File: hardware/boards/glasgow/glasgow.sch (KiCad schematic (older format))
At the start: 89 parts, among them J1 USB_B_Micro, U1 CY7C68013A-56LTX, U15 TPD3S014, U2 CAT24M01W, U3 CAT24C256W, U30 ICE40HX8K-BG121, U34 ATECC508A, U7 LM3880MF-1AF, U8 MIC5355-S4YMME, Y1 24M

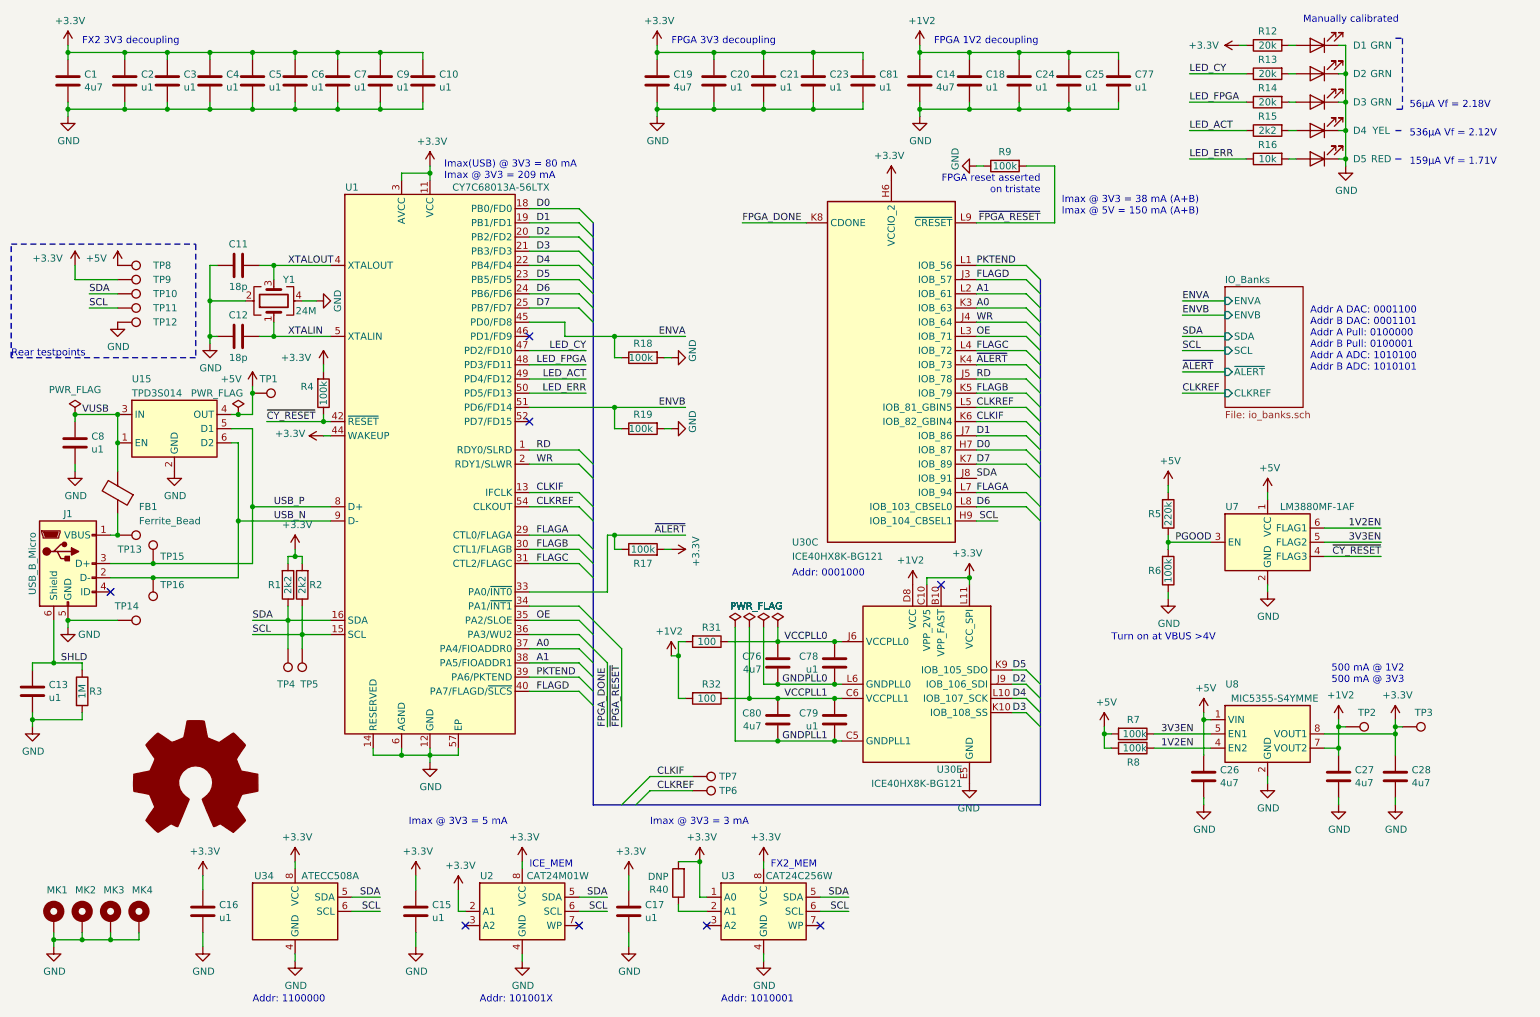
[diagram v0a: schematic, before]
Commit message: revC: add a few detailed explanations on schematic.
Also, where applicable, move text to match moved symbols, and remove
clearly outdated text.
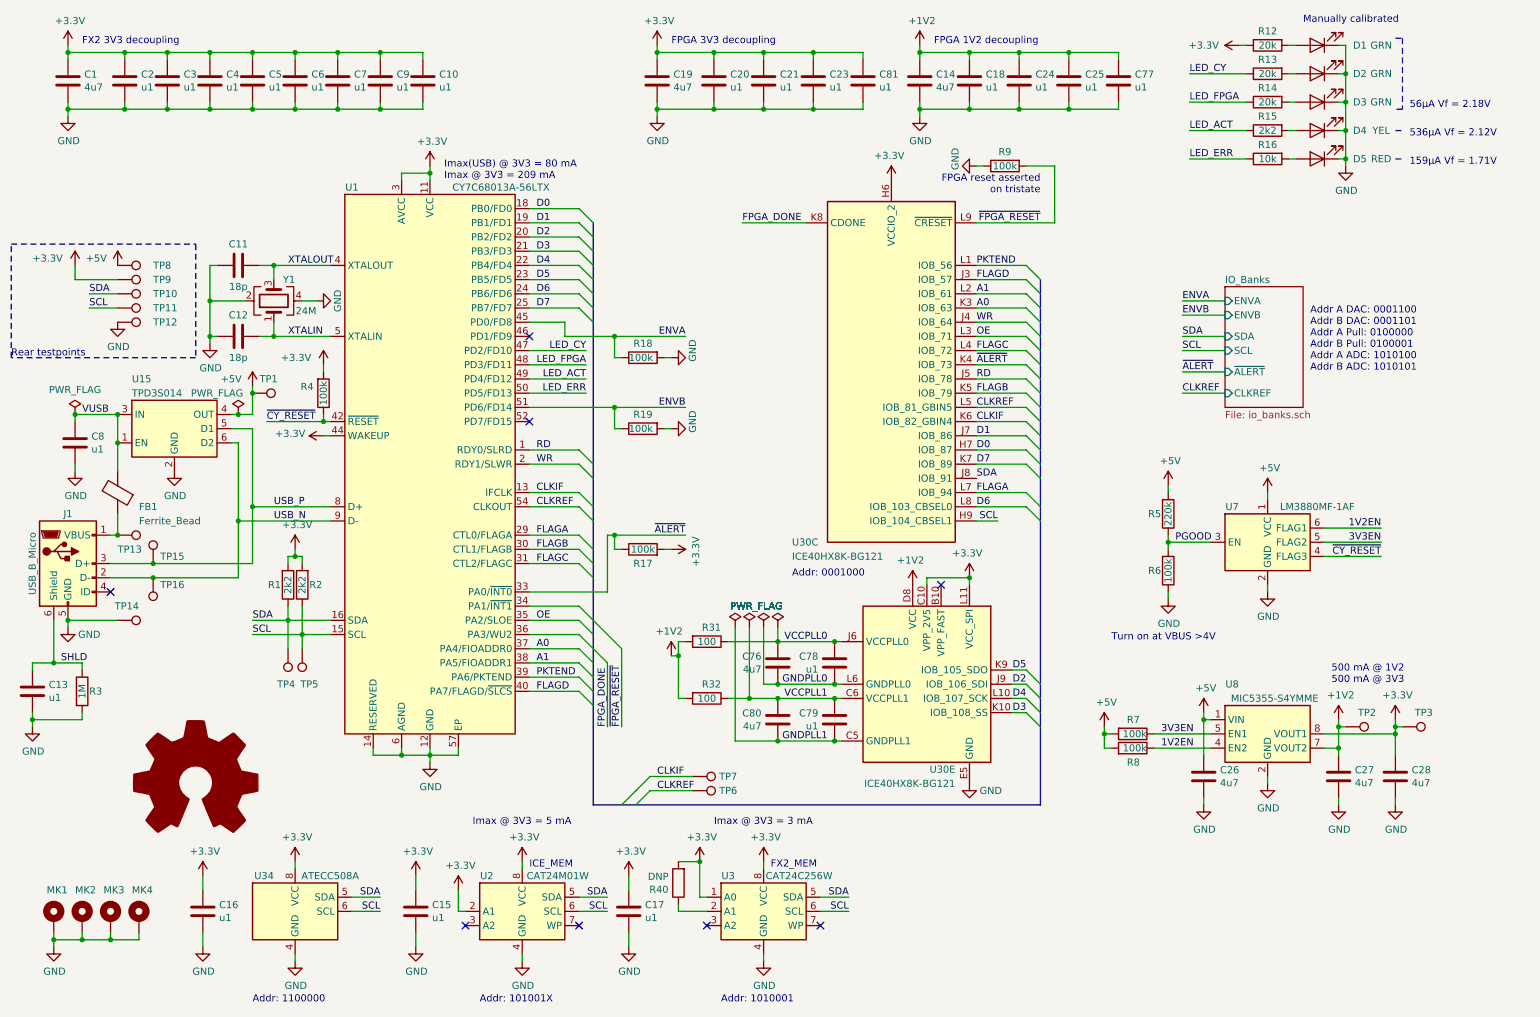
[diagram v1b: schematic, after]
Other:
- note removed: "Imax @ 3V3 = 38 mA (A+B)\nImax @ 5V = 150 mA (A+B)"
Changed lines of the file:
@@
 EESchema Schematic File Version 4
 LIBS:glasgow-cache
-EELAYER 26 0
+EELAYER 29 0
 EELAYER END
 $Descr A4 11693 8268
@@
 Text Notes 7850 1950 2    50   ~ 0
 FPGA reset asserted\non tristate
-Text Notes 3400 6400 0    50   ~ 0
+Text Notes 3850 6400 0    50   ~ 0
 Imax @ 3V3 = 5 mA
-Text Notes 5100 6400 0    50   ~ 0
+Text Notes 5550 6400 0    50   ~ 0
 Imax @ 3V3 = 3 mA
 Text Notes 3650 1850 0    50   ~ 0
 Imax(USB) @ 3V3 = 80 mA\nImax @ 3V3 = 209 mA
-Text Notes 8000 2100 0    50   ~ 0
-Imax @ 3V3 = 38 mA (A+B)\nImax @ 5V = 150 mA (A+B)
 $Comp
 L Connector:TestPoint TP4
@@
 U 5 1 5BD3E8C6
 P 7050 5400
-F 0 "U30" H 6800 4800 50  0000 L CNN
-F 1 "ICE40HX8K-BG121" H 6800 4700 50  0000 L CNN
+F 0 "U30" H 6850 4800 50  0000 L CNN
+F 1 "ICE40HX8K-BG121" H 6850 4700 50  0000 L CNN
 F 2 "Package_BGA:BGA-121_9.0x9.0mm_Layout11x11_P0.8mm_Ball0.4mm_Pad0.35mm_NSMD" H 7050 3950 50  0001 C CNN
 F 3 "http://www.latticesemi.com/Products/FPGAandCPLD/iCE40" H 6200 6400 50  0001 C CNN
@@
 P 7350 6100
 F 0 "#PWR0101" H 7350 5850 50  0001 C CNN
-F 1 "GND" H 7355 5927 50  0000 C CNN
+F 1 "GND" H 7200 6050 50  0000 C CNN
 F 2 "" H 7350 6100 50  0001 C CNN
 F 3 "" H 7350 6100 50  0001 C CNN
@@
 Wire Wire Line
 	1350 4950 1000 4950
+Connection ~ 1000 4950
 Wire Bus Line
 	4700 6250 7850 6250
@@
 Wire Bus Line
 	7850 2550 7850 6250
-Connection ~ 1000 4950
 $EndSCHEMATC

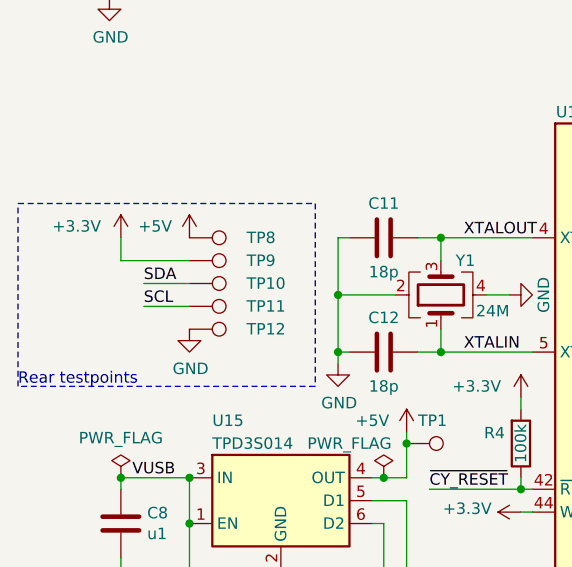
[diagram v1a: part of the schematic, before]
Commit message: revC1: add 1V2 testpoint to the rear
Also fix some testpoint value tags
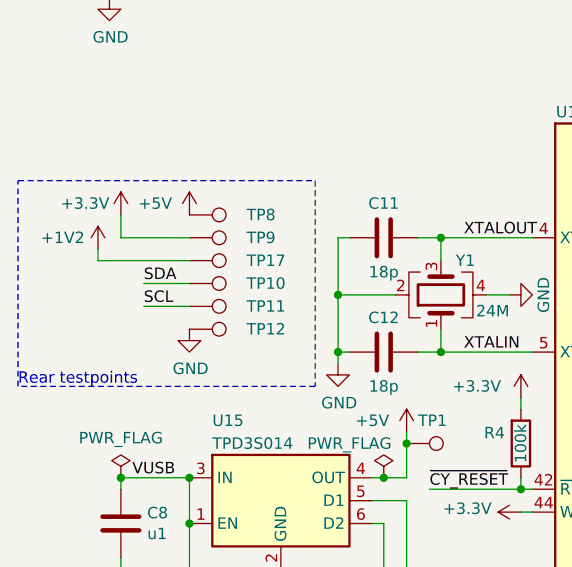
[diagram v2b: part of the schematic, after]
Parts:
- added TP17: 1V2, TestPoint:TestPoint_Pad_D1.0mm, symbol Connector:TestPoint
- TP11: value SDA -> SCL
- TP12: value SDA -> GND
- TP8: value SDA -> 5V
- TP9: value SDA -> 3V3
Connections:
- net +1V2: now also TP17.1
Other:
- moved on the sheet: TP8, TP9
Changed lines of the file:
@@
 L Connector:TestPoint TP8
 U 1 1 5CA9B5FE
+P 1350 2350
+F 0 "TP8" V 1350 2600 50  0000 L CNN
+F 1 "5V" V 1454 2424 50  0001 C CNN
+F 2 "TestPoint:TestPoint_Pad_D1.0mm" H 1550 2350 50  0001 C CNN
+F 3 "~" H 1550 2350 50  0001 C CNN
+	1    1350 2350
+	0    1    1    0
+$EndComp
+$Comp
+L Connector:TestPoint TP9
+U 1 1 5CA9CCBA
 P 1350 2450
-F 0 "TP8" V 1350 2700 50  0000 L CNN
-F 1 "SDA" V 1454 2524 50  0001 C CNN
+F 0 "TP9" V 1350 2700 50  0000 L CNN
+F 1 "3V3" V 1454 2524 50  0001 C CNN
 F 2 "TestPoint:TestPoint_Pad_D1.0mm" H 1550 2450 50  0001 C CNN
 F 3 "~" H 1550 2450 50  0001 C CNN
 	1    1350 2450
-	0    1    1    0
-$EndComp
-$Comp
-L Connector:TestPoint TP9
-U 1 1 5CA9CCBA
-P 1350 2550
-F 0 "TP9" V 1350 2800 50  0000 L CNN
-F 1 "SDA" V 1454 2624 50  0001 C CNN
-F 2 "TestPoint:TestPoint_Pad_D1.0mm" H 1550 2550 50  0001 C CNN
-F 3 "~" H 1550 2550 50  0001 C CNN
-	1    1350 2550
 	0    1    1    0
 $EndComp
@@
 P 1350 2750
 F 0 "TP11" V 1350 3000 50  0000 L CNN
-F 1 "SDA" V 1454 2824 50  0001 C CNN
+F 1 "SCL" V 1454 2824 50  0001 C CNN
 F 2 "TestPoint:TestPoint_Pad_D1.0mm" H 1550 2750 50  0001 C CNN
 F 3 "~" H 1550 2750 50  0001 C CNN
@@
 P 1350 2850
 F 0 "TP12" V 1350 3100 50  0000 L CNN
-F 1 "SDA" V 1454 2924 50  0001 C CNN
+F 1 "GND" V 1454 2924 50  0001 C CNN
 F 2 "TestPoint:TestPoint_Pad_D1.0mm" H 1550 2850 50  0001 C CNN
 F 3 "~" H 1550 2850 50  0001 C CNN
@@
 L power:+5V #PWR0134
 U 1 1 5CB37530
-P 1350 2450
-F 0 "#PWR0134" H 1350 2300 50  0001 C CNN
-F 1 "+5V" H 1200 2500 50  0000 C CNN
-F 2 "" H 1350 2450 50  0001 C CNN
-F 3 "" H 1350 2450 50  0001 C CNN
-	1    1350 2450
+P 1350 2350
+F 0 "#PWR0134" H 1350 2200 50  0001 C CNN
+F 1 "+5V" H 1200 2400 50  0000 C CNN
+F 2 "" H 1350 2350 50  0001 C CNN
+F 3 "" H 1350 2350 50  0001 C CNN
+	1    1350 2350
 	1    0    0    -1
 $EndComp
@@
 L power:+3.3V #PWR041
 U 1 1 5CB375E7
-P 1050 2450
-F 0 "#PWR041" H 1050 2300 50  0001 C CNN
-F 1 "+3.3V" H 750 2500 50  0000 L CNN
-F 2 "" H 1050 2450 50  0001 C CNN
-F 3 "" H 1050 2450 50  0001 C CNN
-	1    1050 2450
+P 1050 2350
+F 0 "#PWR041" H 1050 2200 50  0001 C CNN
+F 1 "+3.3V" H 1000 2400 50  0000 R CNN
+F 2 "" H 1050 2350 50  0001 C CNN
+F 3 "" H 1050 2350 50  0001 C CNN
+	1    1050 2350
 	1    0    0    -1
 $EndComp
 Wire Notes Line
-	600  2300 1900 2300
+	600  2200 1900 2200
 Wire Notes Line
-	1900 2300 1900 3100
+	1900 2200 1900 3100
 Wire Notes Line
 	1900 3100 600  3100
 Wire Notes Line
-	600  3100 600  2300
+	600  3100 600  2200
 Text Notes 600  3100 0    50   ~ 0
 Rear testpoints
 Wire Wire Line
-	1050 2450 1050 2550
-Wire Wire Line
-	1050 2550 1350 2550
+	1050 2350 1050 2450
+Wire Wire Line
+	1050 2450 1350 2450
 NoConn ~ 7150 4700
 $Comp
@@
 	1350 4950 1000 4950
 Connection ~ 1000 4950
+$Comp
+L power:+1V2 #PWR0142
+U 1 1 5CC9337B
+P 950 2500
+F 0 "#PWR0142" H 950 2350 50  0001 C CNN
+F 1 "+1V2" H 1200 2550 50  0000 R CNN
+F 2 "" H 950 2500 50  0001 C CNN
+F 3 "" H 950 2500 50  0001 C CNN
+	1    950  2500
+	-1   0    0    -1
+$EndComp
+Wire Wire Line
+	950  2550 1350 2550
+Wire Wire Line
+	950  2500 950  2550
 Wire Bus Line
 	4700 6250 7850 6250
 Wire Bus Line
+	7850 2550 7850 6250
+Wire Bus Line
 	4700 2150 4700 6250
-Wire Bus Line
-	7850 2550 7850 6250
+$Comp
+L Connector:TestPoint TP17
+U 1 1 5CC2ABF8
+P 1350 2550
+F 0 "TP17" V 1350 2800 50  0000 L CNN
+F 1 "1V2" V 1454 2624 50  0001 C CNN
+F 2 "TestPoint:TestPoint_Pad_D1.0mm" H 1550 2550 50  0001 C CNN
+F 3 "~" H 1550 2550 50  0001 C CNN
+	1    1350 2550
+	0    1    1    0
+$EndComp
 $EndSCHEMATC

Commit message: revC1: Added BOM management keys to the schematic.
This is needed for 1BitSquared production management.
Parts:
- C1, C14, C19, C26, C27, C28, C76, C80: 1b2-bom-key (none) -> cap-cer-0603-4u7
- C10, C13, C15, C16, C17, C18, C2, C20, C21, C23, C24, C25, C3, C4, C5, C6, C7, C77, C78, C79, C8, C81, C9: 1b2-bom-key (none) -> cap-cer-0402-100n
- C11, C12: 1b2-bom-key (none) -> cap-cer-0402-18p
- D1, D2, D3: 1b2-bom-key (none) -> led-0603-grn
- D4: 1b2-bom-key (none) -> led-0603-yel
- D5: 1b2-bom-key (none) -> led-0603-red
- FB1: 1b2-bom-key (none) -> ferrite-0402-600
- J1: 1b2-bom-key (none) -> conn-smd-usb-micro-b
- R1, R15, R2: 1b2-bom-key (none) -> res-0402-2k2
- R12, R13, R14: 1b2-bom-key (none) -> res-0402-20k
- R16: 1b2-bom-key (none) -> res-0402-10k
- R17, R18, R19, R4, R6, R7, R8, R9: 1b2-bom-key (none) -> res-0402-100k
- R3: 1b2-bom-key (none) -> res-0402-1m
- R31, R32: 1b2-bom-key (none) -> res-0402-100
- R5: 1b2-bom-key (none) -> res-0402-220k
- U1: 1b2-bom-key (none) -> ic-cy7c68013a-56ltx
- U15: 1b2-bom-key (none) -> ic-sot23-6-tpd3s014
- U2: 1b2-bom-key (none) -> ic-soic8-cat24m01w
- U3: 1b2-bom-key (none) -> ic-soic8-cat24c256w
- U30: 1b2-bom-key (none) -> ic-ice40hx8k-bg121
- U34: 1b2-bom-key (none) -> ic-wdfn8-atecc508a
- U7: 1b2-bom-key (none) -> ic-sot23-6-lm3880mf-1af
- U8: 1b2-bom-key (none) -> ic-msop8-mic5355-s4ymme
- Y1: 1b2-bom-key (none) -> xtal-lfxtal-24mhz

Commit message: revC1: Updated part information and datasheet links
 - Added resistor network datasheet/part number
 - Updated blue, white, pink LED datasheet/part numbers
 - Updated capacitor datasheets/part numbers
 - Updated resistor part numbers
 - Added MPN/Mfg fields for
	* PCA6408APW
	* SN74LVC1T45DRL
	* ATECC508A
	* MG2040
	* ESD5Z5.0T1G
 - Added information for ferrite bead (600 ohm jellybean)
 - Fixed typo (MG2048 -> MG2040)
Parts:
- C10, C13, C15, C16, C17, C18, C2, C20, C21, C23, C24, C25, C3, C4, C5, C6, C7, C77, C8, C81, C9: MPN TMK107BJ154KA-T -> TMK105BJ104KV-F
- C11, C12: MPN CC0603JRNPO8BN180 -> CC0402JRNPO8BN180
- C78, C79: MPN LMK107BJ475KAHT -> TMK105BJ104KV-F
- FB1: MPN (none) -> BLM15PX601SZ1D; Mfg (none) -> Murata Electronics
- R1, R2: MPN RC0603FR-132K2L -> RC0402FR-132K2L
- R12, R13, R14: MPN RC0603FR-132K2L -> RC0402FR-1320KL
- R15: MPN RC0603FR-13390RL -> RC0402FR-132k2L
- R16: MPN RC0603FR-07604RL -> RC0402FR-1310KL
- R17, R18, R19, R4, R6, R7, R8, R9: MPN RC0603FR-10100KL -> RC0402FR-13100KL
- R3, R40: MPN RC0603FR-131ML -> RC0402FR-131ML
- R31, R32: MPN RC0603FR-07100RL -> RC0402FR-13100RL
- R5: MPN RC0603FR-10220KL -> RC0402FR-13220KL
- U34: MPN (none) -> ATECC508A; Mfg (none) -> Microchip

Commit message: revC1: increase mounting hole size from 3.2mm to 3.5mm, add courtyard space around
- 3.2mm is the standard mounting hole size for M3 screws. But this requires tight
  tolerances that sometimes are difficult to achieve with hobbyist tools. 3.5mm
  allows for more tolerance

- a M3 washer has 7mm outer diameter. A 3mm screw+washer can be offset 0.5mm in a
  3.5mm hole -> 8mm space necessary around the center of the hole. Add 1mm
  clearance + tolerance around gives a 10mm diameter courtyard keepout zone

- change to a pad style with small vias in it because the vias slightly increase
  the adhesion of the copper to the FR4 material. I think it also looks nice.
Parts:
- MK1, MK2, MK3, MK4: footprint MountingHole:MountingHole_3.2mm_M3_Pad -> Glasgow:MountingHole_3.5mm_Pad_Via_CrtYd
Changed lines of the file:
@@
 F 0 "MK1" H 850 7250 50  0000 L CNN
 F 1 "Mounting_Hole_PAD" H 1000 7010 50  0001 L CNN
-F 2 "MountingHole:MountingHole_3.2mm_M3_Pad" H 900 7050 50  0001 C CNN
+F 2 "Glasgow:MountingHole_3.5mm_Pad_Via_CrtYd" H 900 7050 50  0001 C CNN
 F 3 "" H 900 7050 50  0001 C CNN
 	1    900  7050
@@
 F 0 "MK2" H 1050 7250 50  0000 L CNN
 F 1 "Mounting_Hole_PAD" H 1200 7010 50  0001 L CNN
-F 2 "MountingHole:MountingHole_3.2mm_M3_Pad" H 1100 7050 50  0001 C CNN
+F 2 "Glasgow:MountingHole_3.5mm_Pad_Via_CrtYd" H 1100 7050 50  0001 C CNN
 F 3 "" H 1100 7050 50  0001 C CNN
 	1    1100 7050
@@
 F 0 "MK3" H 1250 7250 50  0000 L CNN
 F 1 "Mounting_Hole_PAD" H 1400 7010 50  0001 L CNN
-F 2 "MountingHole:MountingHole_3.2mm_M3_Pad" H 1300 7050 50  0001 C CNN
+F 2 "Glasgow:MountingHole_3.5mm_Pad_Via_CrtYd" H 1300 7050 50  0001 C CNN
 F 3 "" H 1300 7050 50  0001 C CNN
 	1    1300 7050
@@
 F 0 "MK4" H 1450 7250 50  0000 L CNN
 F 1 "Mounting_Hole_PAD" H 1600 7010 50  0001 L CNN
-F 2 "MountingHole:MountingHole_3.2mm_M3_Pad" H 1500 7050 50  0001 C CNN
+F 2 "Glasgow:MountingHole_3.5mm_Pad_Via_CrtYd" H 1500 7050 50  0001 C CNN
 F 3 "" H 1500 7050 50  0001 C CNN
 	1    1500 7050

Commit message: revC1: add Vio active LEDs, misc fixes
- Move some vias that were gratuitously intruding into pads
- Update footprints that changed names upstream
- Beauty fixes
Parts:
- D1, D2, D3, D4, D5: footprint LED_SMD:LED_0603_1608Metric_Pad0.82x1.00mm_HandSolder -> LED_SMD:LED_0603_1608Metric_Pad1.05x0.95mm_HandSolder
- Y1: footprint Crystals:Crystal_SMD_3225-4pin_3.2x2.5mm -> Crystal:Crystal_SMD_3225-4Pin_3.2x2.5mm
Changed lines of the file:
@@
 F 0 "D1" H 9500 900 50  0000 C CNN
 F 1 "GRN" H 9350 900 50  0000 C CNN
-F 2 "LED_SMD:LED_0603_1608Metric_Pad0.82x1.00mm_HandSolder" H 9800 900 50  0001 C CNN
+F 2 "LED_SMD:LED_0603_1608Metric_Pad1.05x0.95mm_HandSolder" H 9800 900 50  0001 C CNN
 F 3 "https://www.mouser.com/datasheet/2/445/150060GS75000-368921.pdf" H 9800 900 50  0001 C CNN
 F 4 "Wurth Electronics" H -450 0   50  0001 C CNN "Mfg"
@@
 F 0 "D2" H 9500 1100 50  0000 C CNN
 F 1 "GRN" H 9350 1100 50  0000 C CNN
-F 2 "LED_SMD:LED_0603_1608Metric_Pad0.82x1.00mm_HandSolder" H 9800 1100 50  0001 C CNN
+F 2 "LED_SMD:LED_0603_1608Metric_Pad1.05x0.95mm_HandSolder" H 9800 1100 50  0001 C CNN
 F 3 "https://www.mouser.com/datasheet/2/445/150060GS75000-368921.pdf" H 9800 1100 50  0001 C CNN
 F 4 "Wurth Electronics" H -450 0   50  0001 C CNN "Mfg"
@@
 F 0 "D3" H 9500 1300 50  0000 C CNN
 F 1 "GRN" H 9350 1300 50  0000 C CNN
-F 2 "LED_SMD:LED_0603_1608Metric_Pad0.82x1.00mm_HandSolder" H 9800 1300 50  0001 C CNN
+F 2 "LED_SMD:LED_0603_1608Metric_Pad1.05x0.95mm_HandSolder" H 9800 1300 50  0001 C CNN
 F 3 "https://www.mouser.com/datasheet/2/445/150060GS75000-368921.pdf" H 9800 1300 50  0001 C CNN
 F 4 "Wurth Electronics" H -450 0   50  0001 C CNN "Mfg"
@@
 F 0 "D4" H 9500 1500 50  0000 C CNN
 F 1 "YEL" H 9350 1500 50  0000 C CNN
-F 2 "LED_SMD:LED_0603_1608Metric_Pad0.82x1.00mm_HandSolder" H 9800 1500 50  0001 C CNN
+F 2 "LED_SMD:LED_0603_1608Metric_Pad1.05x0.95mm_HandSolder" H 9800 1500 50  0001 C CNN
 F 3 "https://www.mouser.com/datasheet/2/445/150060YS75000-368983.pdf" H 9800 1500 50  0001 C CNN
 F 4 "Wurth Electronics" H -450 0   50  0001 C CNN "Mfg"
@@
 F 0 "D5" H 9500 1700 50  0000 C CNN
 F 1 "RED" H 9350 1700 50  0000 C CNN
-F 2 "LED_SMD:LED_0603_1608Metric_Pad0.82x1.00mm_HandSolder" H 9800 1700 50  0001 C CNN
+F 2 "LED_SMD:LED_0603_1608Metric_Pad1.05x0.95mm_HandSolder" H 9800 1700 50  0001 C CNN
 F 3 "https://www.mouser.com/datasheet/2/445/150060RS75000-368563.pdf" H 9800 1700 50  0001 C CNN
 F 4 "Wurth Electronics" H -450 0   50  0001 C CNN "Mfg"
@@
 F 0 "Y1" V 2600 2550 50  0000 L CNN
 F 1 "24M" V 2350 2400 50  0000 L TNN
-F 2 "Crystals:Crystal_SMD_3225-4pin_3.2x2.5mm" H 2450 2700 50  0001 C CNN
+F 2 "Crystal:Crystal_SMD_3225-4Pin_3.2x2.5mm" H 2450 2700 50  0001 C CNN
 F 3 "https://www.mouser.com/datasheet/2/741/LFXTAL058124Reel-940455.pdf" H 2450 2700 50  0001 C CNN
 F 4 "IQD" H 650 -250 50  0001 C CNN "Mfg"
